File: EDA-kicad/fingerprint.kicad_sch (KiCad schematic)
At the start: 1 part, among them J4 FINGER

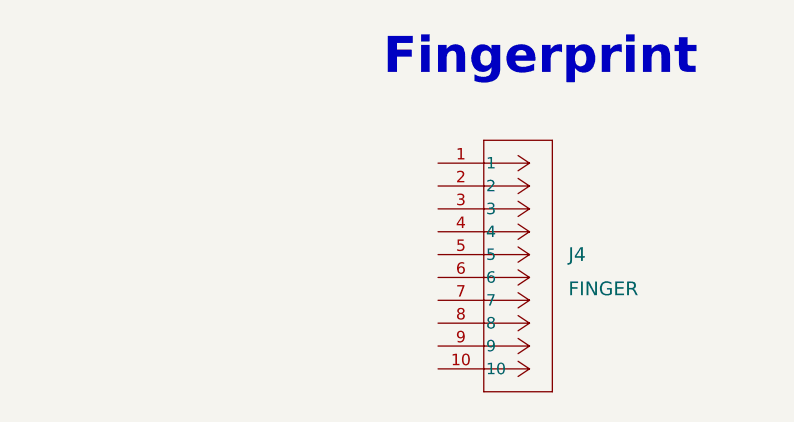
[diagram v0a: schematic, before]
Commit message: finger print scanner connected
missing pin 6 and 7, and we still need a 3d model of the connector for the board

link to datasheet: https://mm.digikey.com/Volume0/opasdata/d220001/medias/docus/5676/SPC26627-3_BM-LITE_Safetouch_Spec.pdf
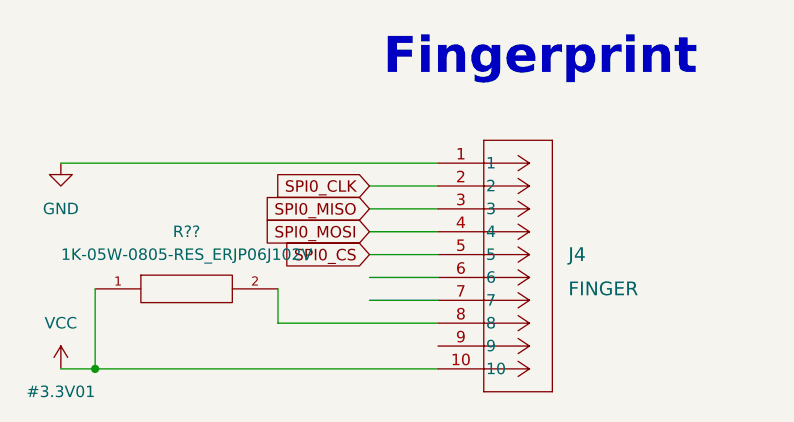
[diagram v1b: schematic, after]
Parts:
- added R??: 1K-05W-0805-RES_ERJP06J102V, SPIRIT-footprints:1K-05W-0805-RES_ERJP06J102V, symbol SPIRIT-components:1K-05W-0805-RES_ERJP06J102V
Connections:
- net GND: now reaches J4.1
- net VCC: now reaches J4.10
- net VCC: now also R??.1
- net SPI0_CLK: now reaches J4.2
- net SPI0_MISO: now reaches J4.3
- net SPI0_MOSI: now reaches J4.4
- net SPI0_CS: now reaches J4.5
- net at J4.8: now also R??.2

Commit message: schematic cleaned up a bit
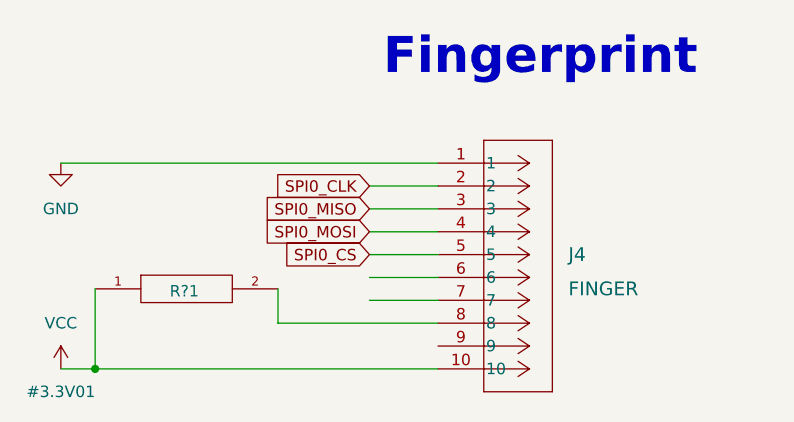
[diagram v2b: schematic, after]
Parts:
- gave numbers to parts that had none: 1
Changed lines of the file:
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@@
 		(on_board yes)
 		(dnp no)
-		(fields_autoplaced yes)
-		(property "Reference" "R??"
-			(at 101.6 101.6 0)
+		(property "Reference" "R?1"
+			(at 101.346 108.204 0)
 			(effects
 				(font
@@
 					(size 1.27 1.27)
 				)
+				(hide yes)
 			)
 		)
@@
 			(project "cm5-carrier"
 				(path "/28c5e4fe-1ec7-4477-97f0-d2ec1401fad5/22a7f479-b60d-43d3-acd2-a72a0c1ab82c"
-					(reference "R??")
+					(reference "R?1")
 					(unit 1)
 				)

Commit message: and here is fingerprint sch
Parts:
- R?1: value 1K-05W-0805-RES_ERJP06J102V -> 270K-05W-0805-RES_ERJP06J102V
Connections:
- net VCC: now also J4.7
- net SPI0_RDY: now reaches J4.6
- no-connect marks 0 -> 1
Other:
- moved on the sheet: R?1
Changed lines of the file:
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@@
+	)
+	(junction
+		(at 91.44 111.76)
+		(diameter 0)
+		(color 0 0 0 0)
 	)
 	(junction
@@
 		(color 0 0 0 0)
 	)
+	(no_connect
+		(at 129.54 114.3)
+	)
 	(wire
 		(pts
@@
 	(wire
 		(pts
-			(xy 91.44 107.95) (xy 91.44 116.84)
+			(xy 91.44 111.76) (xy 91.44 116.84)
 		)
 		(stroke
@@
 	(wire
 		(pts
-			(xy 121.92 109.22) (xy 129.54 109.22)
+			(xy 87.63 93.98) (xy 129.54 93.98)
 		)
 		(stroke
@@
 	(wire
 		(pts
-			(xy 87.63 93.98) (xy 129.54 93.98)
+			(xy 91.44 109.22) (xy 129.54 109.22)
 		)
 		(stroke
@@
 	(wire
 		(pts
-			(xy 91.44 116.84) (xy 129.54 116.84)
+			(xy 91.44 109.22) (xy 91.44 111.76)
 		)
 		(stroke
@@
 	(wire
 		(pts
-			(xy 121.92 99.06) (xy 129.54 99.06)
+			(xy 91.44 116.84) (xy 129.54 116.84)
 		)
 		(stroke
@@
 	(wire
 		(pts
-			(xy 121.92 106.68) (xy 129.54 106.68)
+			(xy 121.92 99.06) (xy 129.54 99.06)
 		)
 		(stroke
@@
 	(wire
 		(pts
-			(xy 111.76 111.76) (xy 129.54 111.76)
+			(xy 121.92 106.68) (xy 129.54 106.68)
 		)
 		(stroke
@@
 	(wire
 		(pts
-			(xy 111.76 107.95) (xy 111.76 111.76)
+			(xy 111.76 111.76) (xy 129.54 111.76)
 		)
 		(stroke
@@
 		)
 	)
+	(global_label "SPI0_RDY"
+		(shape input)
+		(at 121.92 106.68 180)
+		(fields_autoplaced yes)
+		(effects
+			(font
+				(size 1.27 1.27)
+			)
+			(justify right)
+		)
+		(property "Intersheetrefs" "${INTERSHEET_REFS}"
+			(at 110.0448 106.68 0)
+			(effects
+				(font
+					(size 1.27 1.27)
+				)
+				(justify right)
+				(hide yes)
+			)
+		)
+	)
 	(global_label "SPI0_MISO"
 		(shape input)
@@
 	(symbol
 		(lib_id "SPIRIT-components:1K-05W-0805-RES_ERJP06J102V")
-		(at 101.6 107.95 0)
+		(at 101.6 111.76 0)
 		(unit 1)
 		(exclude_from_sim no)
@@
 		(dnp no)
 		(property "Reference" "R?1"
-			(at 101.346 108.204 0)
-			(effects
-				(font
-					(size 1.27 1.27)
-				)
-			)
-		)
-		(property "Value" "1K-05W-0805-RES_ERJP06J102V"
-			(at 101.6 104.14 0)
+			(at 101.346 112.014 0)
+			(effects
+				(font
+					(size 1.27 1.27)
+				)
+			)
+		)
+		(property "Value" "270K-05W-0805-RES_ERJP06J102V"
+			(at 101.6 107.95 0)
 			(effects
 				(font
@@
 		)
 		(property "Footprint" "SPIRIT-footprints:1K-05W-0805-RES_ERJP06J102V"
-			(at 101.6 107.95 0)
+			(at 101.6 111.76 0)
 			(effects
 				(font
@@
 		)
 		(property "Datasheet" ""
-			(at 101.6 107.95 0)
+			(at 101.6 111.76 0)
 			(effects
 				(font
@@
 		)
 		(property "Description" ""
-			(at 101.6 107.95 0)
+			(at 101.6 111.76 0)
 			(effects
 				(font
@@
 		)
 		(property "PARTREV" "3/1/2020"
-			(at 101.6 107.95 0)
+			(at 101.6 111.76 0)
 			(effects
 				(font
@@
 		)
 		(property "STANDARD" "Manufacturer Recommendations"
-			(at 101.6 107.95 0)
+			(at 101.6 111.76 0)
 			(effects
 				(font
@@
 		)
 		(property "MAXIMUM_PACKAGE_HEIGHT" "0.6 mm"
-			(at 101.6 107.95 0)
+			(at 101.6 111.76 0)
 			(effects
 				(font
@@
 		)
 		(property "MANUFACTURER" "Panasonic"
-			(at 101.6 107.95 0)
-			(effects
-				(font
+			(at 101.6 111.76 0)
+			(effects
+				(font

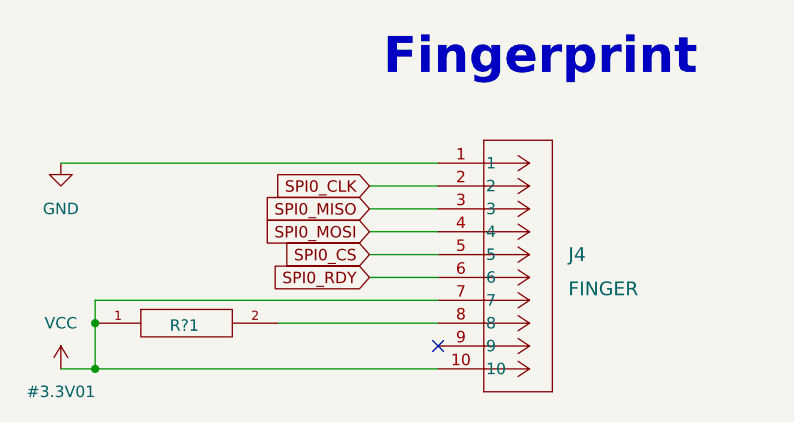
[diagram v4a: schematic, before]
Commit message: fully sync pcb to schematic, fix some models
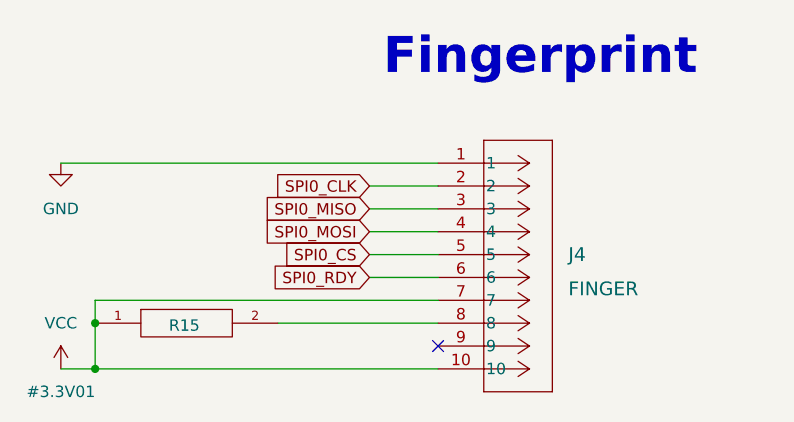
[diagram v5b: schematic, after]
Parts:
- renumbered R?1 to R15
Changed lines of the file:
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@@
 			"AAAAQwAAAGoAAABTAAAAUwAAAFQAAABhAAAATgAAAGoAAABqAAAAZQAAAGoAAABqAAAASgAAAGoA"
 			"AABtAAAAZQAAAGUAAAByAAAAdAAAAGUAAABWAAAAeAAAAGQAAAB6AAAAOQAAAHYAAABWAAAAeAAA"
-			"AGIAAABPAAAAWQAAAHgAAABWAAAARgAAAEEAAABDAAAAQwAAADQAAA=="
+			"AGIAAABPAAAAWQAAAHgAAABWAAAARgAAAEEAAABDAAAAQwAAADQAAAAAAAAAAAAAABDManQOVgAA"
+			"YEHWcQ5WAABoQdZxDlYAAGhB1nEOVgAAnHpJcLAVmsGwJdB2DlYAAAEAAAAAAAAAMQAAAAAAAABX"
+			"bGRHZVZWcgAAAAAAAAAAAAAAAAAAAAABAAAAUnpsNVQybE5kMDFFAAAAAFJFRTMAAAAAAAAAAOAl"
+			"0HYOVgAA4CXQdg5WAAAAAAAAAAAAAMDibHAOVgAAQJPbdA5WAABIk9t0DlYAAEiT23QOVgAAnHpJ"
+			"cLAVmsFAJtB2DlYAAAEAAAAAAAAAMQAAAAAAAABZMGRHYW1GWQAAAAAAAAAAAAAAAAAAAAABAAAA"
+			"VjNoc1QyMDFkbUp1AAAAAGJUZzMAAAAAAAAAAHAm0HYOVgAAcCbQdg5WAAAAAAAAAAAAADCeSm8O"
+			"VgAA8F3Lgg5WAAAAXsuCDlYAAABey4IOVgAAA5nAZv7j8wTQJtB2DlYAAAEAAAAAAAAAMgAAAAAA"
+			"AABZa2RzZFZwWAAAAAAAAAAAAAAAAAAAAAACAAAATTFKNVlqSjBiRXhYAAAAAFIxWjUAAAAAAAAA"
+			"AAAn0HYOVgAAACfQdg5WAAAAAAAAAAAAACDYDnIOVgAAUOGShw5WAABg4ZKHDlYAAGDhkocOVgAA"
+			"A5nAZv7j8wRgJ9B2DlYAAAEAAAAAAAAAMgAAAAAAAABZVEpWZEdJegAAAAAAAAAAAAAAAAAAAAAC"
+			"AAAAYlhSc1kycHdkV0l5AAAAAE1rNTIAAAAAAAAAAJAn0HYOVgAAkCfQdg5WAAAAAAAAAAAAANB3"
+			"N3oOVgAAsGnshw5WAADAaeyHDlYAAMBp7IcOVgAAA5nAZv7j8wTwJ9B2DlYAAAEAAAAAAAAAMgAA"
+			"AAAAAABXbnB3YUdSWQAAAAAAAAAAAAAAAAAAAAACAAAAUjFaNVlWYzFiazl0AAAAAFJ6ZzMAAAAA"
+			"AAAAACAo0HYOVgAAICjQdg5WAAAAAAAAAAAAAFBaqGgOVgAAcOmQhw5WAACA6ZCHDlYAAIDpkIcO"
+			"VgAAA5nAZv7j8wSAKNB2DlYAAAEAAAAAAAAAMgAAAAAAAABUVk0wTVUxRQAAAAAAAAAAAAAAAAAA"
+			"AAACAAAAZVhjeFRHcEJlRTVVAAAAAFF6QjUAAAAAAAAAALAo0HYOVgAAsCjQdg5WAAAAAAAAAAAA"
+			"ANAA3HEOVgAAAEzlaA5WAAAQTOVoDlYAABBM5WgOVgAA/4yZBJbZyxAQKdB2DlYAAAEAAAAAAAAA"
+			"MwAAAAAAAABUa04zZEU1cAAAAAAAAAAAAAAAAAAAAAADAAAAUTBGblNVTkJaMkZYAAAAAGJrSm8A"
+			"AAAAAAAAAEAp0HYOVgAAQCnQdg5WAAAAAAAAAAAAAAAMYXYOVgAAcP//////////////////////"
+			"////////////////////////////////////////////////////////////////////////////"
+			"////////////////////////////////////////////////////////////////////////////"
+			"////////////////////////////////////////////////////////////////////////////"
+			"////////////////////////////////////////////////////////////////////////////"
+			"////////////////////////////////////////////////////////////////////////////"
+			"////////////////////////////////////////////////////////////////////////////"
+			"////////////////////////////////////////////////////////////////////////////"
+			"////////////////////////////////////////////////////////////////////////////"
+			"////////////////////////////////////////////////////////////////////////////"
+			"////////////////////////////////////////////////////////////////////////////"
+			"////////////////////////////////////////////////////////////////////////////"
+			"////////////////////////////////////////////////////////////////////////////"
+			"////////////////////////////////////////////////////////////////////////////"
+			"////////////////////////////////////////////////////////////////////////////"
+			"////////////////////////////////////////////////////////////////////////////"
+			"////////////////////////////////////////////////////////////////////////////"
+			"////////////////////////////////////////////////////////////////////////////"
+			"/////////////////////////////////////////////////////w=="
 		)
 	)
@@
 			"1frGRFOgKNhoG7Hbd1Dhrt21dHpUisS3bB5wMjNPeevsuQKn09U2MgQAZvyl3/DETiPHrPJsU6mW"
 			"utqD/OmuFF8axq5LUABO/7Mpecbx9uK4hZxTO26uldMSycoEbdD97S9kF81f9N+CQvu0mVu63N6s"
-			"RXN/ALrzjub/emdwbl7pK9M2Xvc51XWYWhlhg8SBj7Ea6NBWAAAg3BtbOxkRwr2xrA=="
+			"RXN/ALrzjub/emdwbl7pK9M2Xvc51XWYWhlhg8SBj7Ea6NBWAAAg3BtbOxkRwr2xrICzrI5x0/wV"
+			"1qrQc8XA7JqPHuo6+70AXAhxzN/B23VYcQXKTFX+vuomVtiZcKX943qkBhgCDAAK4mlLtpZG4fOa"
+			"JnRYc71sTlabm7R5SMcCN9YrdG7+oXClwJVrh3tr3HvkL14C4FGPwsl6IgYvElqP3YSE33JNjjP5"
+			"2IxmzRhU3le2JCEzLZw8VncSPwtQOkPKzb8aeMYPI94ZLN8lq9WMY0drW5+PJ1AK4+qy0Gb1dq3w"
+			"7Me3yuUOJTqjTP1HrWeewPkhUSEcmn9oQwX+tvYOKXWk08MjS/ESAI86uk7UawMwRiJWrAvHRfOv"
+			"AG5cViKTkpSZFjo9pXsZBgtRTkhxuzoIr6oyeNVg+TppofFQlRPGcKfCX4mY192u+YcwYOAnt2Z2"
+			"GdiWY3WnxhWsQLd3UHXJ/MN5et9KbvTWu/fIN7wEwAOALpP0flXuiHWMi+b/tRgUL702O+abj6TT"
+			"E3qwAeVAq1SaP/A/hZvfHyzTkpSYNMeN0m7i40WCqxI6Mf+wzU01fo5ec7P82yWZtmg1WvcvqGY5"
+			"cIhj87c+oDxQSfG6UvnDlkgPjyzEmwnQg64T9Von5q+RodjmP68JtM9W8z/1SW1twHJSbP4K84wA"
+			"bdNh/gAf3SqvGgbdga0umT9Ai4IA410R6IAvh8h/jQDnGvCz1THqzPxROMfXhCWHPagH2Rbq4ZFl"
+			"eDUADZwzJuqhAp8KNLc6Jp75xyoI260RGL50IKOzdSWxU8frQYFqlgIHOzH/OAa7DeGO926Ux2xI"
+			"dMyxj+rFArNQ8+TfZo/6fh/fmp5EJhatH9Z2PoMlwK7h5Qklaol/n7+q0ueru2SxPZUeHtmDVwPQ"
+			"wPHBsFSbv8B/DeiytERGZav5nzRODwxU8xYpNH+tneDouEyZP8DqW2SOKn+JLI+qxYFEzR+UUcc9"
+			"qqbzRKSTL4bKxyr0ALYCtVX+7po/wO4ivNrqPr3VgVQPj6zASwAaMIWlWoDF1L51huD0zV9Y4qvh"
+			"xBUlstyuzlTTfrzu64c3iNeGTILmH+2mCoza+hud3r1BvrQt1CVW38J9wNzQvuk/Kbke9XsYNdzl"
+			"kjxHrB0mb4lwHsrmuN9l3Y8YcdMdClR4pOX9+ny7h3UHe0o9PDKPlwA0YIx9OYqI6lJIaMhazILg"
+			"roowcp9dOGvJ9fKjA5kppf143aNxNYtRjnDN/OuzSaHXe4PltjWlWTK7oYhWNaEv8JkL5l+7KQxu"
+			"O1pbxjo8XawZJsvUx/mA5dBSN/q0CFy6rZq3W96rh9sW6+GRQbwEoAEjBewRWZaU+ZvUGwd3NyAU"
+			"LR0ow2f1kgBZSuGjuktBNYsV2sbrIGbH/FX43BA6vD9YXnSm1H3WXC+bDR+XABvrBf//////////"
+			"////////////////////////////////////////////////////////////////////////////"
+			"////////////////////////////////////////////////////////////////////////////"
+			"////////////////////////////////////////////////////////////////////////////"
+			"////////////////////////////////////////////////////////////////////////////"
+			"////////////////////////////////////////////////////////////////////////////"
+			"////////////////////////////////////////////////////////////////////////////"
+			"////////////////////////////////////////////////////////////////////////////"
+			"////////////////////////////////////////////////////////////////////////////"
+			"////////////////////////////////////////////////////////////////////////////"
+			"////////////////////////////////////////////////////////////////////////////"
+			"////////////////////////////////////////////////////////////////////////////"
+			"////////////////////////////////////////////////////////////////////////////"
+			"////////////////////////////////////////////////////////////////////////////"
+			"////////////////////////////////////////////////////////////////////////////"
+			"////////////////////////////////////////////////////////////////////////////"
+			"////////////////////////////////////////////////////////////////////////////"
+			"////////////////////////////////////////////////////////////////////////////"
+			"/////////////////////////////////////////////////////////////////w=="
 		)
 	)
@@
 		(on_board yes)
 		(dnp no)
-		(property "Reference" "R?1"
+		(property "Reference" "R15"
 			(at 101.346 112.014 0)
 			(effects
@@
 			(project "cm5-carrier"
 				(path "/28c5e4fe-1ec7-4477-97f0-d2ec1401fad5/22a7f479-b60d-43d3-acd2-a72a0c1ab82c"
-					(reference "R?1")
+					(reference "R15")
 					(unit 1)
 				)
